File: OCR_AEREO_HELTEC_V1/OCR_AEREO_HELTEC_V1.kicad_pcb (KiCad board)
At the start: 2 copper layers, 109.5 x 85.5 mm, 39 parts, among them J1 Conn_01x04_Socket, J10 Conn_01x02_Pin, J11 Conn_01x02_Pin, J12 Conn_01x08_Socket, J14 MODULO SD, J2 Conn_01x04_Socket, J3 Conn_01x18_Pin, J4 Conn_01x02_Pin, J5 Conn_01x02_Pin, J6 OCR, J7 BATERÍA, J8 Conn_01x02_Pin, J9 Conn_01x02_Pin, U2 MAX3232

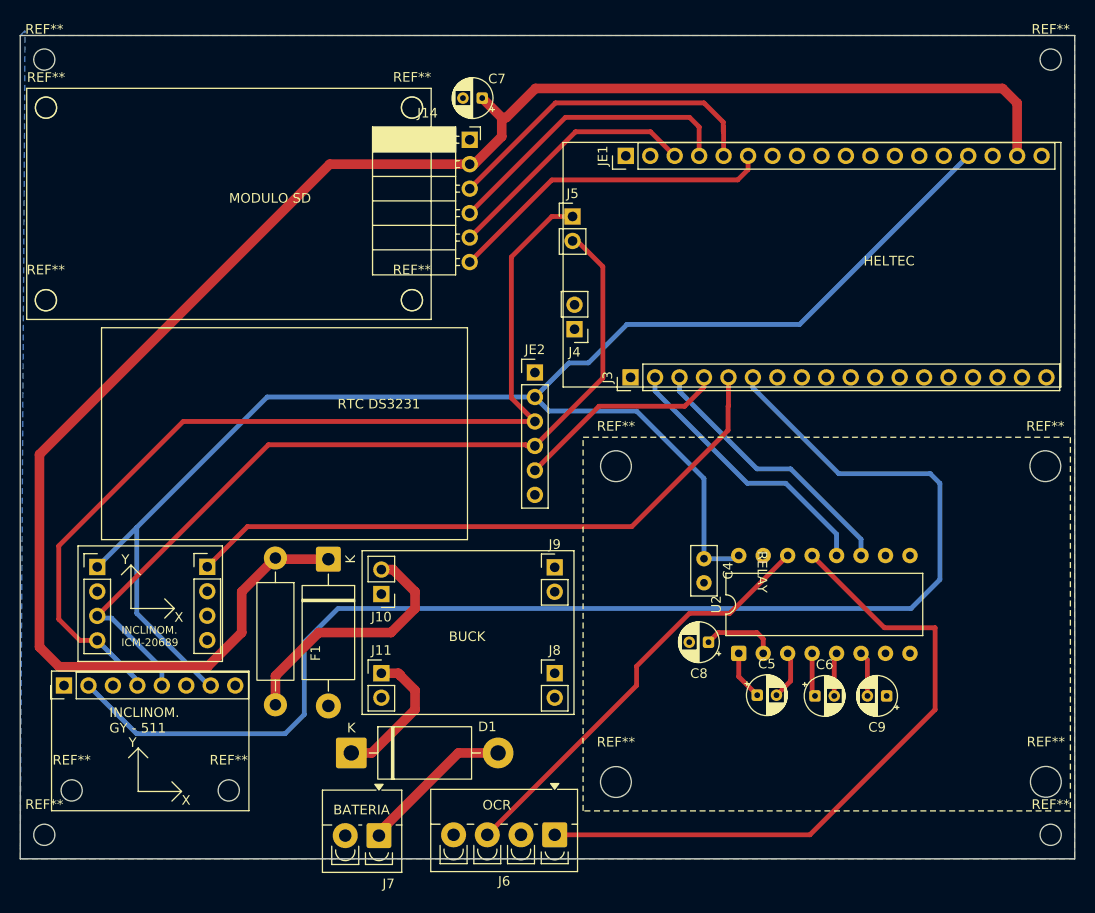
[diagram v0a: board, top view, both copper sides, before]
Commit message: pcb corregida
rtc, buck y relay . distancias corregidas
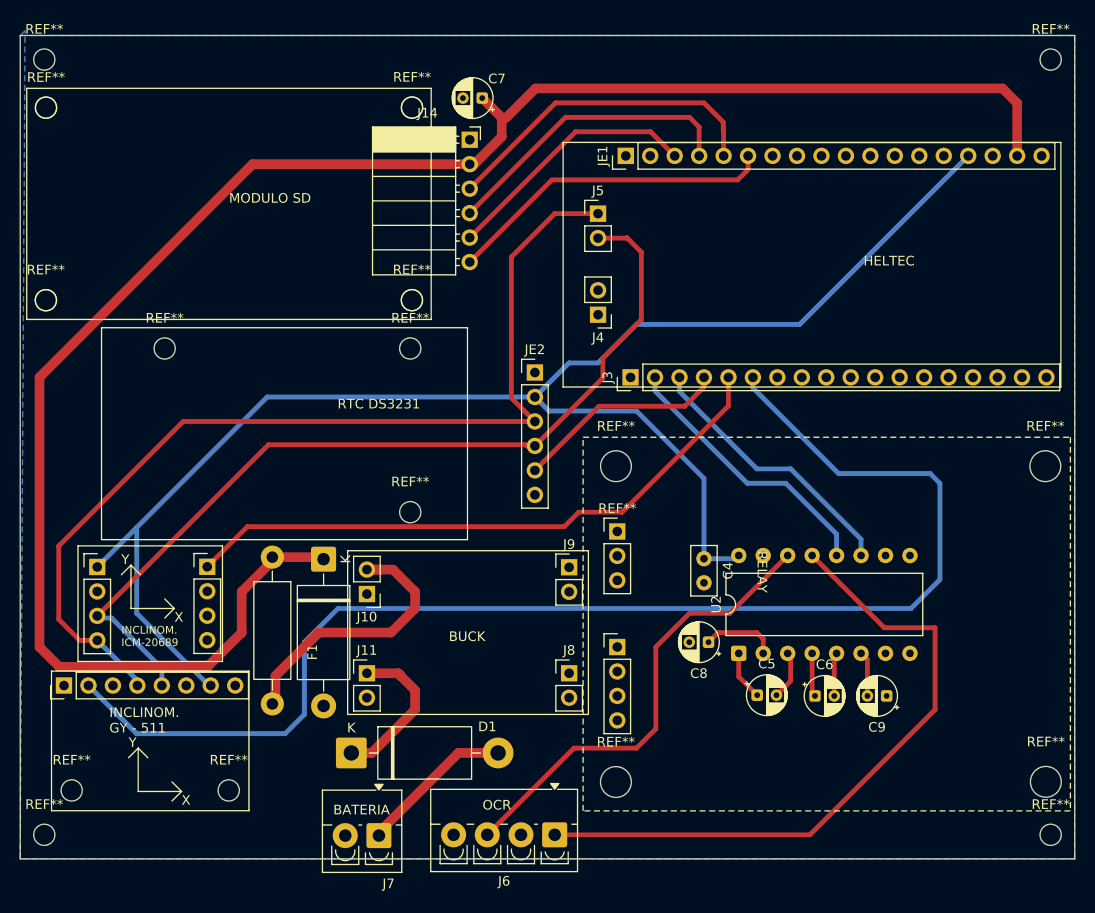
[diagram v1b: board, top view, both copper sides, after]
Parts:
- added J1: Conn_01x04_Socket, Connector_PinHeader_2.54mm:PinHeader_1x04_P2.54mm_Vertical, F.Cu at (102.0, 103.5)
- added REF**: MountingHole_2.2mm_M2, MountingHole:MountingHole_2.2mm_M2, F.Cu at (80.5, 89.5)
- added REF**: PinHeader_1x03_P2.54mm_Vertical, Connector_PinHeader_2.54mm:PinHeader_1x03_P2.54mm_Vertical, F.Cu at (102.0, 91.5)
- added REF**: MountingHole_2.2mm_M2, MountingHole:MountingHole_2.2mm_M2, F.Cu at (80.5, 72.5)
- added REF**: MountingHole_2.2mm_M2, MountingHole:MountingHole_2.2mm_M2, F.Cu at (55.0, 72.5)
- moved J4 2.87 mm to (100.0, 69.0)
- moved J5 2.66 mm to (100.0, 58.5)
- moved J10 1.50 mm to (76.0, 98.0)
- moved J11 1.50 mm to (76.0, 106.2)
- moved J8 1.50 mm to (97.0, 106.2)
- moved J9 1.50 mm to (97.0, 95.2)
- moved D2 0.50 mm to (71.5, 94.4)
- moved F1 0.33 mm to (66.2, 94.2)
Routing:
- net 5V: track 186.6 -> 191.3 mm
- net SCL: track 89.4 -> 93.4 mm
- net RX_OCR: track 44.4 -> 48.2 mm
- net SDA: track 100.4 -> 103.6 mm
- net OUT_BUCK: track 26.6 -> 29.6 mm
- net IN_BUCK: track 14.7 -> 16.2 mm
- net INT_INCL_1: track 65.5 -> 64.0 mm

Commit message: archivos de fabricacion
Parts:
- moved J8 1.50 mm to (95.5, 106.2)
- moved J9 1.50 mm to (95.5, 95.2)
